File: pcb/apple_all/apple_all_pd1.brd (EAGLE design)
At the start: 56 x 65 mm, 47 parts, among them IC1 STM32F072C8T6, SW1 324_SW, SW2 324_SW, SW3 324_SW

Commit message: updated PCB
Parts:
- added TP1, TP2, TP3: PTR1TP14R, testpad:TP14R
- moved R11 2.03 mm to (30.0, 22.0)
- moved JP2 1.02 mm to (26.9, 55.9), turned to 270 degrees
- moved U$5 1.02 mm to (16.8, 61.0)
- moved U$6 1.02 mm to (37.1, 61.0)
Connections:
- new net N$10: IC1.41, JP2.2
- new net N$20: IC1.4, TP1.TP
- new net N$41: IC1.5, TP2.TP
- new net N$42: IC1.6, TP3.TP
- net N$24: no longer JP6.SLEEVE-NORM
- net N$46: no longer IC1.41, JP2.2
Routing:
- net N$46: track 126.5 -> 105.1 mm
- net N$10: track 0.00 -> 13.2 mm
- net N$24: track 14.8 -> 3.49 mm
- net N$41: track 0.00 -> 6.28 mm, vias 0 -> 1
- net N$20: track 0.00 -> 4.68 mm, vias 0 -> 1
- net N$42: track 0.00 -> 2.88 mm, vias 0 -> 1
- net N$3: track 57.5 -> 60.0 mm
- net N$43: track 55.1 -> 57.0 mm
- net N$18: track 42.4 -> 43.3 mm
- net N$21: track 10.5 -> 9.69 mm
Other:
- board text added: "PC15"
- board text added: "PF0"
- board text added: "PF1"
- board text removed: "ADBPWR"

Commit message: updated values
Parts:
- R11, R7: value 200 -> 100
- R18, R21, R6, R9: value 2K -> 5.1K
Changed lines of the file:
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@@
 <attribute name="VALUE" x="54.991" y="8.636" size="1.27" layer="27" rot="R90"/>
 </element>
-<element name="R9" library="SparkFun-Passives" package="0805" value="2K" x="49.53" y="9.9822" smashed="yes" rot="R90">
+<element name="R9" library="SparkFun-Passives" package="0805" value="5.1K" x="49.53" y="9.9822" smashed="yes" rot="R90">
 <attribute name="NAME" x="50.3555" y="10.5156" size="0.8128" layer="25" rot="R270"/>
 </element>
@@
 <attribute name="VALUE" x="27.813" y="51.562" size="1.27" layer="27" rot="R180"/>
 </element>
-<element name="R18" library="SparkFun-Passives" package="0805" value="2K" x="26.543" y="46.736" smashed="yes">
+<element name="R18" library="SparkFun-Passives" package="0805" value="5.1K" x="26.543" y="46.736" smashed="yes">
 <attribute name="NAME" x="25.5778" y="44.9707" size="0.8128" layer="25"/>
 </element>
@@
 <attribute name="VALUE" x="29.718" y="46.482" size="1.27" layer="27"/>
 </element>
-<element name="R21" library="SparkFun-Passives" package="0805" value="2K" x="30.988" y="46.736" smashed="yes" rot="R180">
+<element name="R21" library="SparkFun-Passives" package="0805" value="5.1K" x="30.988" y="46.736" smashed="yes" rot="R180">
 <attribute name="NAME" x="30.0228" y="44.9199" size="0.8128" layer="25"/>
 </element>
@@
 <attribute name="VALUE" x="31.75" y="37.719" size="1.27" layer="27" rot="R270"/>
 </element>
-<element name="R7" library="SparkFun-Passives" package="0805" value="200" x="33.909" y="21.971" smashed="yes" rot="R270">
+<element name="R7" library="SparkFun-Passives" package="0805" value="100" x="33.909" y="21.971" smashed="yes" rot="R270">
 <attribute name="NAME" x="34.3535" y="19.05" size="0.8128" layer="25" rot="R90"/>
 </element>
-<element name="R11" library="SparkFun-Passives" package="0805" value="200" x="29.972" y="21.971" smashed="yes" rot="R270">
+<element name="R11" library="SparkFun-Passives" package="0805" value="100" x="29.972" y="21.971" smashed="yes" rot="R270">
 <attribute name="NAME" x="29.6545" y="20.447" size="0.8128" layer="25" rot="R270"/>
 </element>
@@
 <attribute name="VALUE" x="23.749" y="58.42" size="1.27" layer="27" rot="R270"/>
 </element>
-<element name="R6" library="SparkFun-Passives" package="0805" value="2K" x="48.006" y="62.611" smashed="yes" rot="R90">
+<element name="R6" library="SparkFun-Passives" package="0805" value="5.1K" x="48.006" y="62.611" smashed="yes" rot="R90">
 <attribute name="NAME" x="48.895" y="64.8335" size="0.8128" layer="25" rot="R180"/>
 </element>

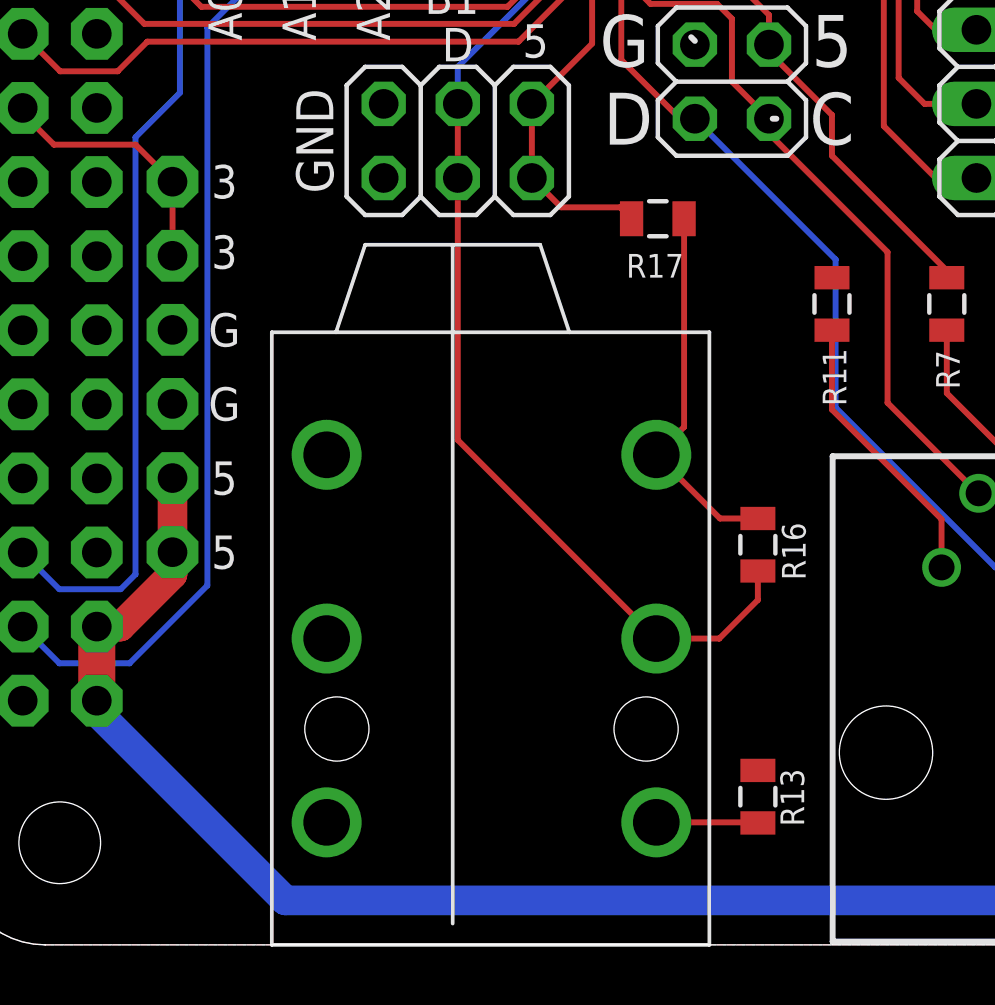
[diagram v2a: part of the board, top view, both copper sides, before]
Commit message: moved resistors
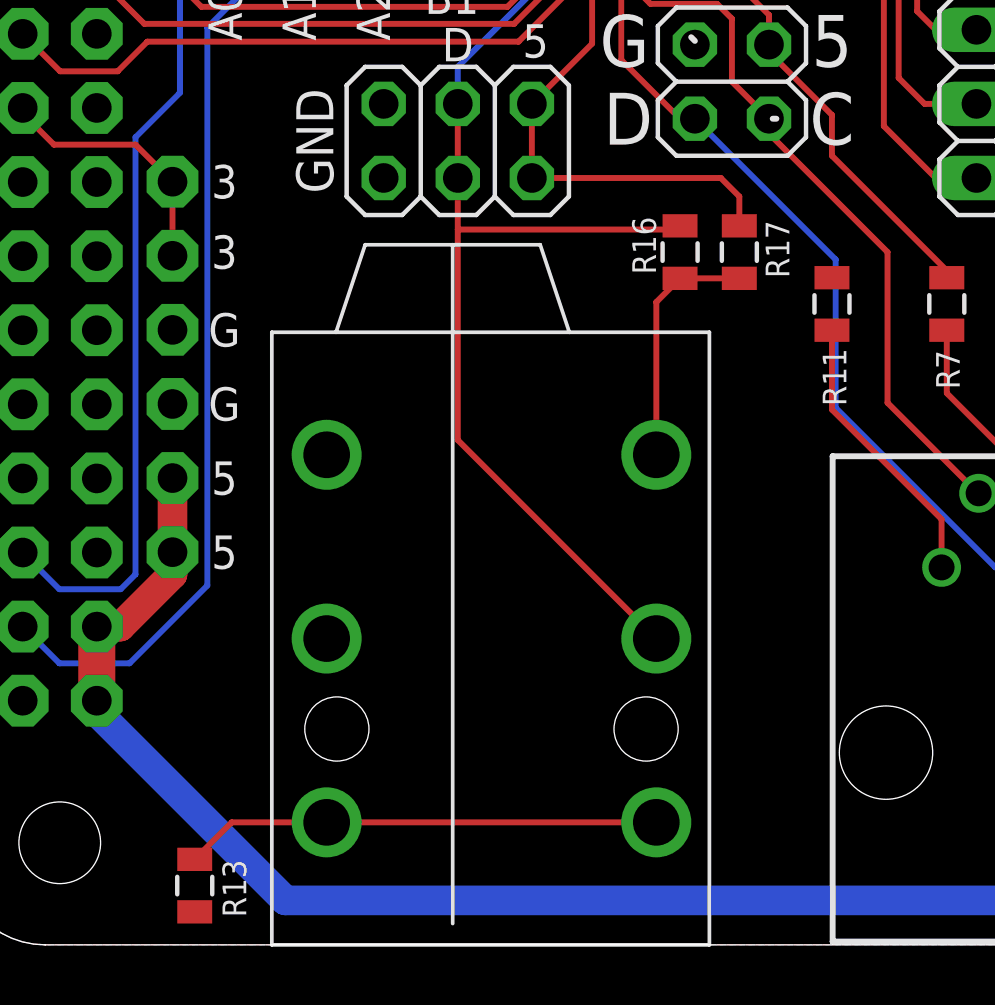
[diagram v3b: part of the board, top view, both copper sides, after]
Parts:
- moved R13 19.5 mm to (8.13, 2.03), turned to 270 degrees
- moved R16 10.4 mm to (24.8, 23.7), turned to 90 degrees
- moved R17 3.02 mm to (26.8, 23.7), turned to 90 degrees
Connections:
- net N$24: now also JP6.SLEEVE-NORM
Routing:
- net N$24: track 3.49 -> 16.3 mm
- net N$32: track 12.9 -> 8.42 mm
- net N$31: track 13.1 -> 17.4 mm
- net N$30: track 36.7 -> 39.4 mm
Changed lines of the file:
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@@
 <attribute name="VALUE" x="13.335" y="23.114" size="1.27" layer="27"/>
 </element>
-<element name="R16" library="SparkFun-Passives" package="0805" value="5.1K" x="27.432" y="13.716" smashed="yes" rot="R270">
-<attribute name="NAME" x="28.2575" y="14.478" size="0.8128" layer="25" rot="R270"/>
-</element>
-<element name="R13" library="SparkFun-Passives" package="0805" value="100" x="27.432" y="5.08" smashed="yes" rot="R90">
-<attribute name="NAME" x="29.0195" y="4.064" size="0.8128" layer="25" rot="R90"/>
+<element name="R16" library="SparkFun-Passives" package="0805" value="5.1K" x="24.765" y="23.749" smashed="yes" rot="R90">
+<attribute name="NAME" x="23.9395" y="22.987" size="0.8128" layer="25" rot="R90"/>
+</element>
+<element name="R13" library="SparkFun-Passives" package="0805" value="100" x="8.128" y="2.032" smashed="yes" rot="R270">
+<attribute name="NAME" x="9.0805" y="2.921" size="0.8128" layer="25" rot="R270"/>
 </element>
 <element name="JP2" library="pinhead" library_urn="urn:adsk.eagle:library:325" package="1X02" package3d_urn="urn:adsk.eagle:package:22435/2" value="" x="26.924" y="55.88" smashed="yes" rot="R270">
@@
 <attribute name="NAME" x="48.895" y="64.8335" size="0.8128" layer="25" rot="R180"/>
 </element>
-<element name="R17" library="SparkFun-Passives" package="0805" value="100" x="24.003" y="24.892" smashed="yes" rot="R180">
-<attribute name="NAME" x="24.892" y="23.6855" size="0.8128" layer="25" rot="R180"/>
+<element name="R17" library="SparkFun-Passives" package="0805" value="100" x="26.797" y="23.749" smashed="yes" rot="R90">
+<attribute name="NAME" x="28.5115" y="22.86" size="0.8128" layer="25" rot="R90"/>
 </element>
 <element name="TP2" library="testpad" library_urn="urn:adsk.eagle:library:385" package="TP14R" package3d_urn="urn:adsk.eagle:package:27966/1" value="PTR1TP14R" x="22.987" y="37.846" smashed="yes" rot="MR0">
@@
 <wire x1="21.75" y1="30.894" x2="21.75" y2="34.5" width="0.2032" layer="1"/>
 <contactref element="R17" pad="2"/>
-<wire x1="19.685" y1="26.289" x2="20.69" y2="25.284" width="0.2032" layer="1"/>
-<wire x1="23.103" y1="24.892" x2="22.711" y2="25.284" width="0.2032" layer="1"/>
-<wire x1="22.711" y1="25.284" x2="20.69" y2="25.284" width="0.2032" layer="1"/>
+<wire x1="19.685" y1="26.289" x2="26.162" y2="26.289" width="0.2032" layer="1"/>
+<wire x1="26.797" y1="25.654" x2="26.797" y2="24.649" width="0.2032" layer="1"/>
+<wire x1="26.162" y1="26.289" x2="26.797" y2="25.654" width="0.2032" layer="1"/>
 </signal>
 <signal name="N$24">
 <contactref element="JP6" pad="SLEEVE"/>
 <contactref element="R13" pad="1"/>
-<wire x1="23.95" y1="4.2" x2="27.412" y2="4.2" width="0.2032" layer="1"/>
-<wire x1="27.412" y1="4.2" x2="27.432" y2="4.18" width="0.2032" layer="1"/>
+<contactref element="JP6" pad="SLEEVE-NORM"/>
+<wire x1="8.128" y1="2.932" x2="9.396" y2="4.2" width="0.2032" layer="1"/>
+<wire x1="9.396" y1="4.2" x2="12.65" y2="4.2" width="0.2032" layer="1"/>
+<wire x1="12.65" y1="4.2" x2="23.95" y2="4.2" width="0.2032" layer="1"/>
 </signal>
 <signal name="N$11">
@@
 <contactref element="JP6" pad="RING"/>
 <contactref element="R16" pad="2"/>
-<wire x1="27.432" y1="12.816" x2="27.432" y2="11.823" width="0.2032" layer="1"/>
-<wire x1="27.432" y1="11.823" x2="26.109" y2="10.5" width="0.2032" layer="1"/>
-<wire x1="26.109" y1="10.5" x2="23.95" y2="10.5" width="0.2032" layer="1"/>
 <contactref element="IC1" pad="13"/>
 <contactref element="JP5" pad="3"/>
@@
 <wire x1="20.32" y1="33.274" x2="17.145" y2="30.099" width="0.2032" layer="16"/>
 <wire x1="17.145" y1="17.305" x2="23.95" y2="10.5" width="0.2032" layer="1"/>
-<wire x1="17.145" y1="26.289" x2="17.145" y2="17.305" width="0.2032" layer="1"/>
+<wire x1="17.145" y1="26.289" x2="17.145" y2="24.522" width="0.2032" layer="1"/>
+<wire x1="17.145" y1="24.522" x2="17.145" y2="17.305" width="0.2032" layer="1"/>
+<wire x1="24.765" y1="24.649" x2="24.638" y2="24.522" width="0.2032" layer="1"/>
+<wire x1="24.638" y1="24.522" x2="17.145" y2="24.522" width="0.2032" layer="1"/>
 </signal>
 <signal name="N$32">
 <contactref element="JP6" pad="TIP"/>
 <contactref element="R16" pad="1"/>
-<wire x1="23.95" y1="16.8" x2="26.134" y2="14.616" width="0.2032" layer="1"/>
-<wire x1="26.134" y1="14.616" x2="27.432" y2="14.616" width="0.2032" layer="1"/>
 <contactref element="R17" pad="1"/>
-<wire x1="24.903" y1="24.892" x2="24.903" y2="17.753" width="0.2032" layer="1"/>
-<wire x1="24.903" y1="17.753" x2="23.95" y2="16.8" width="0.2032" layer="1"/>
+<wire x1="23.95" y1="16.8" x2="23.95" y2="22.034" width="0.2032" layer="1"/>
+<wire x1="23.95" y1="22.034" x2="24.765" y2="22.849" width="0.2032" layer="1"/>
+<wire x1="26.797" y1="22.849" x2="24.765" y2="22.849" width="0.2032" layer="1"/>
 </signal>
 <signal name="N$33">

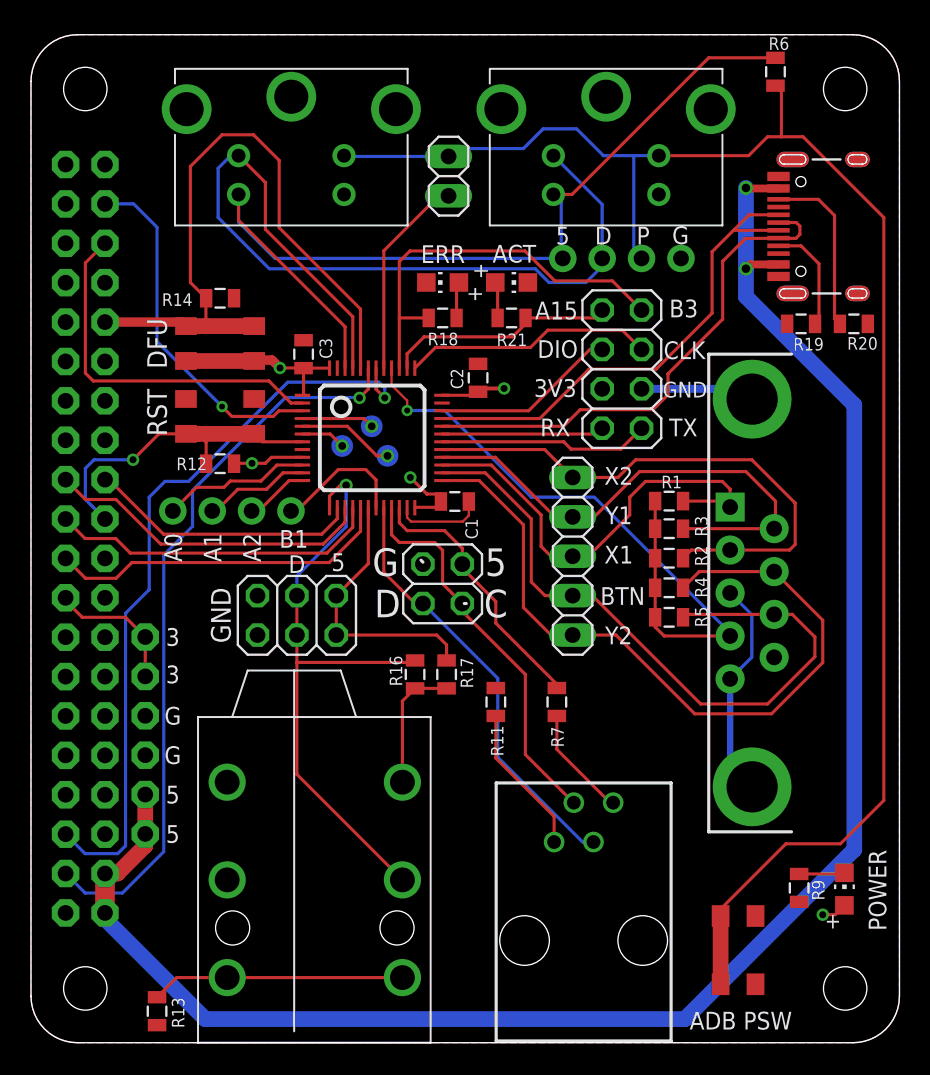
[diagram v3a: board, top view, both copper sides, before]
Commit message: added resistors on DET pins, cleaned up silkscreen
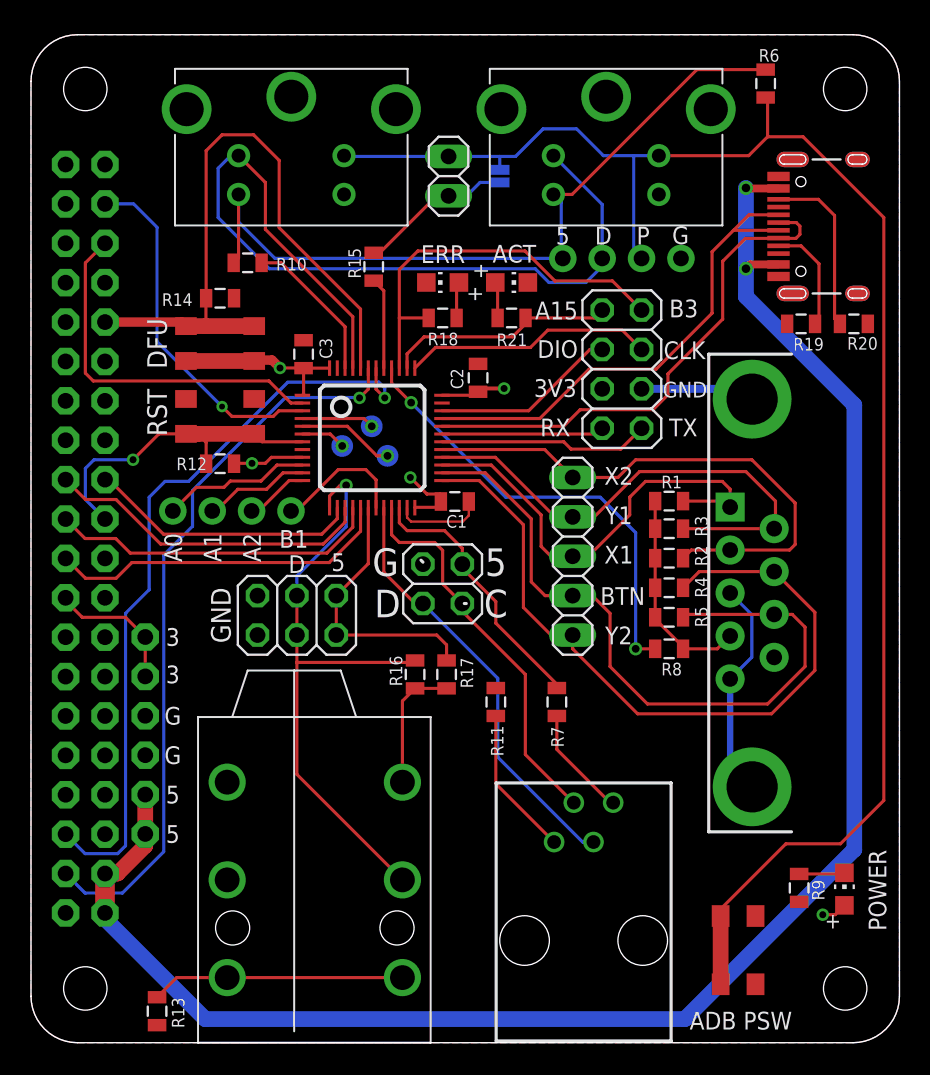
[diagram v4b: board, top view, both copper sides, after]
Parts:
- added JP9: JUMPER-SMT_2_NO_NO-SILK, SparkFun-Jumpers:SMT-JUMPER_2_NO_NO-SILK
- added R10, R15, R8: 100, SparkFun-Passives:0805
- moved R6 0.99 mm to (47.4, 61.8)
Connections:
- new net N$44: IC1.40, R8.1
- new net N$45: IC1.46, R10.1
- new net N$47: JP2.2, JP9.1, R15.2
- net +7V: now also R8.2; no longer IC1.40
- net N$10: now also R15.1; no longer JP2.2
- net N$3: now also R10.2; no longer IC1.46
- net N$46: now also JP9.2
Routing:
- net +7V: track 43.3 -> 13.6 mm, vias 1 -> 0
- net N$44: track 0.00 -> 29.4 mm, vias 0 -> 2
- net N$3: track 60.0 -> 49.6 mm
- net N$47: track 0.00 -> 10.0 mm
- net N$45: track 0.00 -> 9.76 mm
- net N$10: track 13.2 -> 5.91 mm
- net N$4: track 44.3 -> 45.8 mm
- net N$18: track 43.3 -> 42.4 mm
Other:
- board text added: "USB4VC Protocol Card Apple Lisa Early Macintosh Apple Desktop Bus"
- board text removed: "USB4VC Protocol Card for Apple Lisa, Early Macintosh & Apple Desktop Bus"
